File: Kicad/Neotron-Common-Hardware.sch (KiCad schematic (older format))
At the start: 17 parts, among them J101 Neotron-Expansion-Slot, J102 Neotron-Expansion-Slot, J103 Neotron-Expansion-Slot, J104 Neotron-Expansion-Slot, U101 Neotron-CPU

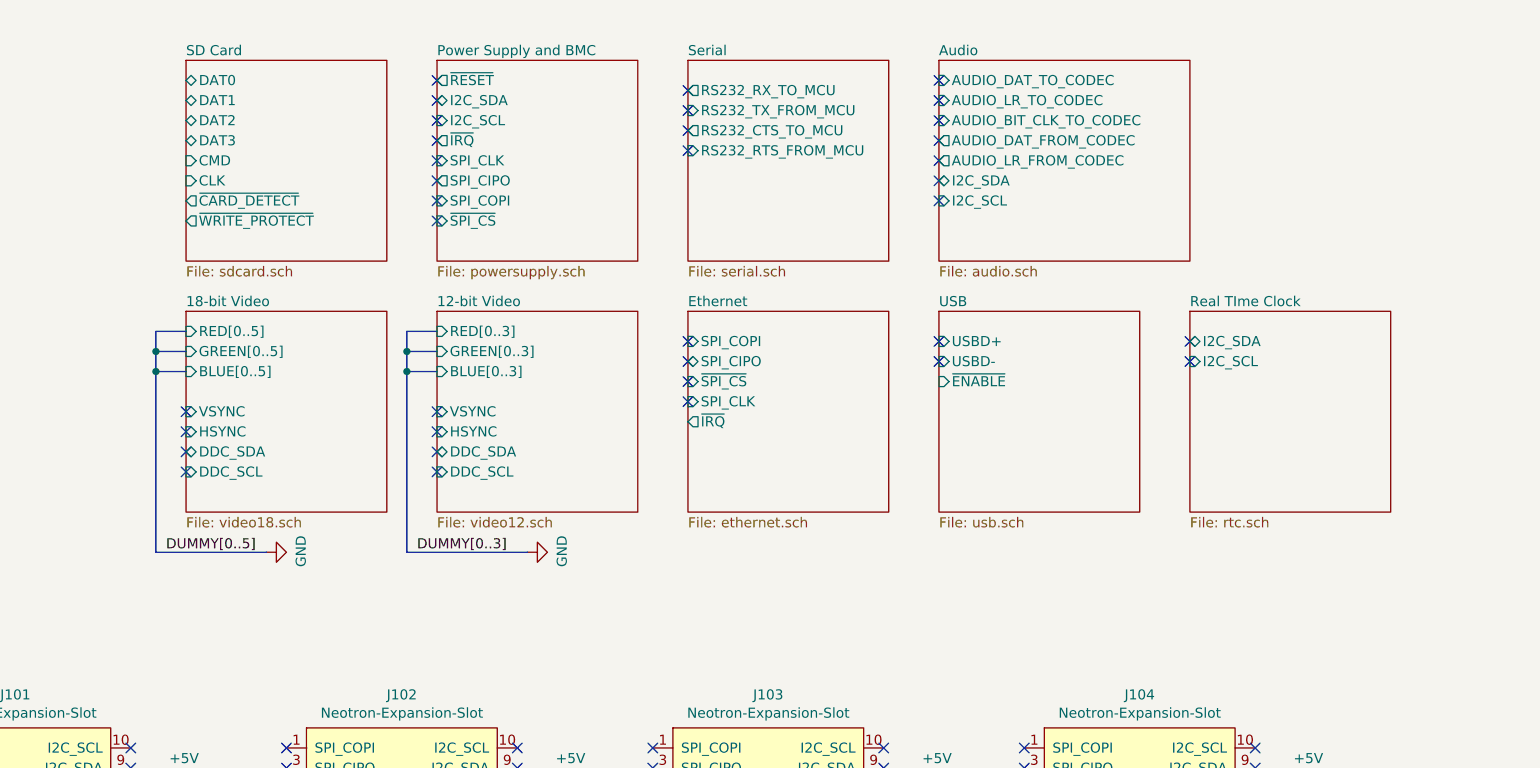
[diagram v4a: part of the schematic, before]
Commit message: Changes to BMC
* Swapped BUTTON_PWR and SYS_RESET to avoid DRC issue
* Split PSU and BMC into two separate sheets
* Swapped some pins on the STM32 to make it compatible with more
alternatives
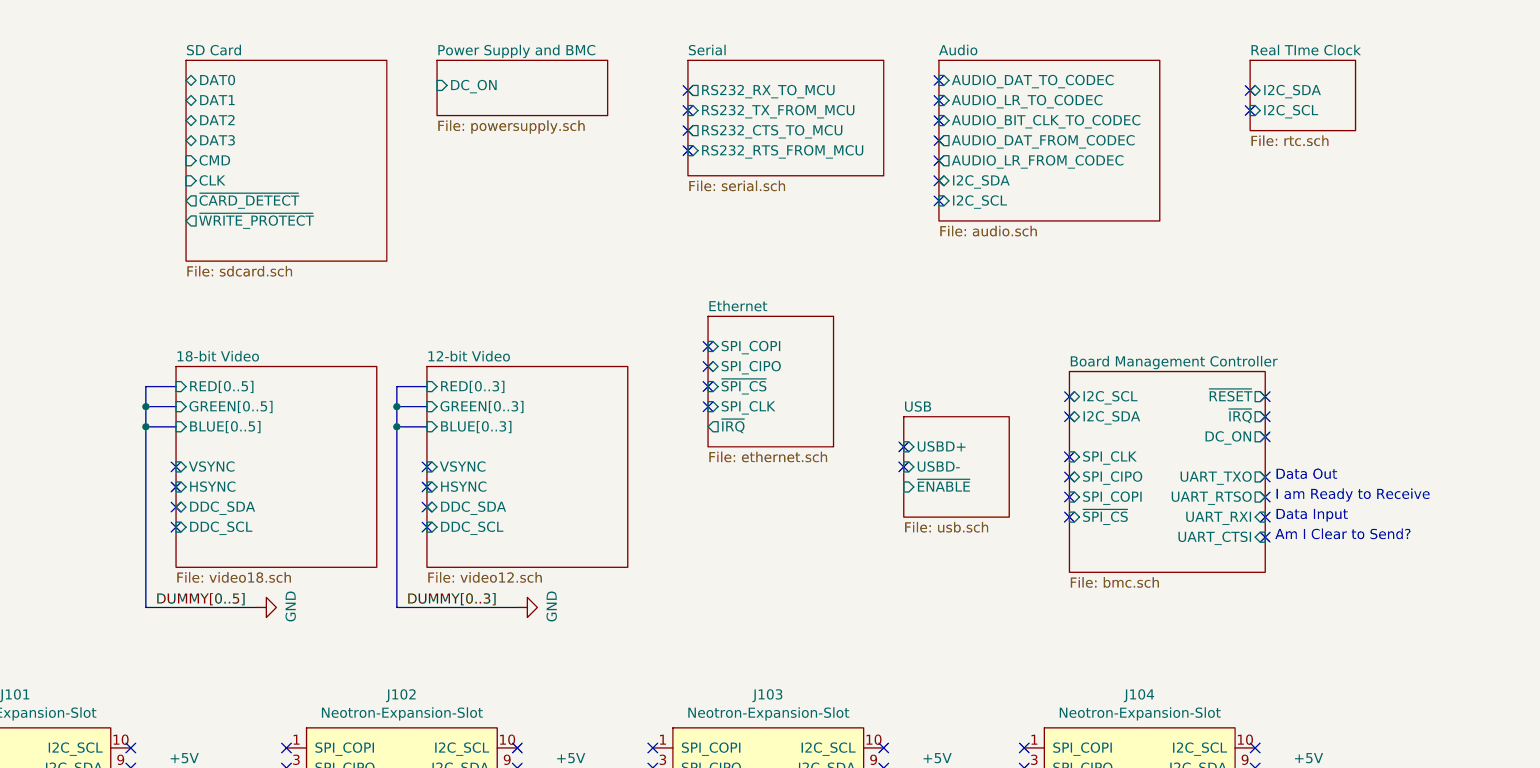
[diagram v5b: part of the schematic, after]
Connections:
- no-connect marks 132 -> 137
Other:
- note added: "Am I Clear to Send?"
- note added: "Data Input"
- note added: "Data Out"
- note added: "I am Ready to Receive"
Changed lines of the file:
@@
 $Descr A4 11693 8268
 encoding utf-8
-Sheet 1 16
+Sheet 1 17
 Title "Neotron Common Hardware"
 Date "2021-04-02"
@@
 $EndDescr
 $Sheet
-S 4850 2050 1000 1000
+S 4800 2325 1000 1000
 U 5FDE658D
 F0 "18-bit Video" 50
 F1 "video18.sch" 50
-F2 "DDC_SDA" B L 4850 2750 50
-F3 "DDC_SCL" I L 4850 2850 50
-F4 "VSYNC" I L 4850 2550 50
-F5 "HSYNC" I L 4850 2650 50
-F6 "RED[0..5]" I L 4850 2150 50
-F7 "GREEN[0..5]" I L 4850 2250 50
-F8 "BLUE[0..5]" I L 4850 2350 50
+F2 "DDC_SDA" B L 4800 3025 50
+F3 "DDC_SCL" I L 4800 3125 50
+F4 "VSYNC" I L 4800 2825 50
+F5 "HSYNC" I L 4800 2925 50
+F6 "RED[0..5]" I L 4800 2425 50
+F7 "GREEN[0..5]" I L 4800 2525 50
+F8 "BLUE[0..5]" I L 4800 2625 50
 $EndSheet
 $Sheet
-S 8600 800  1250 1000
+S 8600 800  1100 800
 U 5FDE6C5A
 F0 "Audio" 50
@@
 NoConn ~ 8600 1400
 NoConn ~ 8600 1500
-NoConn ~ 7350 2300
-NoConn ~ 7350 2400
-NoConn ~ 7350 2500
-NoConn ~ 7350 2200
+NoConn ~ 7450 2325
+NoConn ~ 7450 2425
+NoConn ~ 7450 2525
+NoConn ~ 7450 2225
 $Comp
 L Mechanical:MountingHole_Pad H102
@@
 	1    0    0    -1
 $EndComp
-NoConn ~ 8600 2200
-NoConn ~ 8600 2300
+NoConn ~ 8425 2725
+NoConn ~ 8425 2825
 $Sheet
 S 4850 800  1000 1000
@@
 	-1   0    0    -1
 $EndComp
-NoConn ~ 6100 1200
-NoConn ~ 6100 1100
-NoConn ~ 6100 1000
-NoConn ~ 6100 900
 NoConn ~ 7350 1250
 NoConn ~ 7350 1150
@@
 NoConn ~ 7350 950
 $Sheet
-S 7350 800  1000 1000
+S 7350 800  975  575
 U 5FDF53DB
 F0 "Serial" 50
@@
 $EndSheet
 $Sheet
-S 6100 800  1000 1000
-U 5FDE7599
-F0 "Power Supply and BMC" 50
-F1 "powersupply.sch" 50
-F2 "~RESET" O L 6100 900 50
-F3 "I2C_SDA" B L 6100 1000 50
-F4 "I2C_SCL" I L 6100 1100 50
-F5 "~IRQ" O L 6100 1200 50
-F6 "SPI_CLK" I L 6100 1300 50
-F7 "SPI_CIPO" O L 6100 1400 50
-F8 "SPI_COPI" I L 6100 1500 50
-F9 "~SPI_CS" I L 6100 1600 50
-$EndSheet
-$Sheet
-S 8600 2050 1000 1000
+S 8425 2575 525  500
 U 5FDE7004
 F0 "USB" 50
 F1 "usb.sch" 50
-F2 "USBD+" I L 8600 2200 50
-F3 "USBD-" I L 8600 2300 50
-F4 "~ENABLE" I L 8600 2400 50
+F2 "USBD+" I L 8425 2725 50
+F3 "USBD-" I L 8425 2825 50
+F4 "~ENABLE" I L 8425 2925 50
 $EndSheet
 $Sheet
-S 7350 2050 1000 1000
+S 7450 2075 625  650
 U 5FDE698D
 F0 "Ethernet" 50
 F1 "ethernet.sch" 50
-F2 "SPI_COPI" I L 7350 2200 50
-F3 "~SPI_CS" I L 7350 2400 50
-F4 "SPI_CLK" I L 7350 2500 50
-F5 "~IRQ" O L 7350 2600 50
-F6 "SPI_CIPO" T L 7350 2300 50
+F2 "SPI_COPI" I L 7450 2225 50
+F3 "~SPI_CS" I L 7450 2425 50
+F4 "SPI_CLK" I L 7450 2525 50
+F5 "~IRQ" O L 7450 2625 50
+F6 "SPI_CIPO" T L 7450 2325 50
 $EndSheet
 $Comp
@@
 NoConn ~ 3875 1250
 NoConn ~ 3875 1350
-NoConn ~ 4850 2550
-NoConn ~ 4850 2650
-NoConn ~ 4850 2750
-NoConn ~ 4850 2850
+NoConn ~ 4800 2825
+NoConn ~ 4800 2925
+NoConn ~ 4800 3025
+NoConn ~ 4800 3125
 NoConn ~ 2150 3675
 NoConn ~ 2575 3375
@@
 Connection ~ 4825 4525
 $Comp
-L power:+3V3 #PWR0118
+L power:+3V3 #PWR0117
 U 1 1 5FED8E4E
 P 4975 4625
-F 0 "#PWR0118" H 4975 4475 50  0001 C CNN
+F 0 "#PWR0117" H 4975 4475 50  0001 C CNN
 F 1 "+3V3" H 4990 4798 50  0000 C CNN
 F 2 "" H 4975 4625 50  0001 C CNN
@@
 $EndComp
 $Comp
-L power:GND #PWR0119
+L power:GND #PWR0118
 U 1 1 5FEDE866
 P 5200 5350
-F 0 "#PWR0119" H 5200 5100 50  0001 C CNN
+F 0 "#PWR0118" H 5200 5100 50  0001 C CNN
 F 1 "GND" H 5205 5177 50  0000 C CNN
 F 2 "" H 5200 5350 50  0001 C CNN
@@
 NoConn ~ 6200 6100
 $Sheet
-S 9850 2050 1000 1000
+S 10150 800  525  350
 U 5FEF404D
 F0 "Real TIme Clock" 50
 F1 "rtc.sch" 50
-F2 "I2C_SDA" B L 9850 2200 50
-F3 "I2C_SCL" I L 9850 2300 50
+F2 "I2C_SDA" B L 10150 950 50
+F3 "I2C_SCL" I L 10150 1050 50
 $EndSheet
-NoConn ~ 9850 2200
-NoConn ~ 9850 2300
+NoConn ~ 10150 950
+NoConn ~ 10150 1050
 $Sheet
-S 6100 2050 1000 1000
+S 6050 2325 1000 1000
 U 60677AF0
 F0 "12-bit Video" 50
 F1 "video12.sch" 50
-F2 "DDC_SDA" B L 6100 2750 50
-F3 "DDC_SCL" I L 6100 2850 50
-F4 "VSYNC" I L 6100 2550 50
-F5 "HSYNC" I L 6100 2650 50
-F6 "RED[0..3]" I L 6100 2150 50
-F7 "GREEN[0..3]" I L 6100 2250 50
-F8 "BLUE[0..3]" I L 6100 2350 50
+F2 "DDC_SDA" B L 6050 3025 50
+F3 "DDC_SCL" I L 6050 3125 50
+F4 "VSYNC" I L 6050 2825 50
+F5 "HSYNC" I L 6050 2925 50
+F6 "RED[0..3]" I L 6050 2425 50
+F7 "GREEN[0..3]" I L 6050 2525 50
+F8 "BLUE[0..3]" I L 6050 2625 50
 $EndSheet
-NoConn ~ 6100 2850
-NoConn ~ 6100 2750
-NoConn ~ 6100 2550
-NoConn ~ 6100 2650
+NoConn ~ 6050 3125
+NoConn ~ 6050 3025
+NoConn ~ 6050 2825
+NoConn ~ 6050 2925
 Wire Bus Line
-	6100 2150 5950 2150
+	6050 2425 5900 2425
 Wire Bus Line
-	5950 2150 5950 2250
+	5900 2425 5900 2525
 Wire Bus Line
-	5950 3250 6550 3250
+	5900 3525 6500 3525
 $Comp
 L power:GND #PWR0121
 U 1 1 606B5F3A
-P 6550 3250
-F 0 "#PWR0121" H 6550 3000 50  0001 C CNN
-F 1 "GND" H 6555 3077 50  0000 C CNN
-F 2 "" H 6550 3250 50  0001 C CNN
-F 3 "" H 6550 3250 50  0001 C CNN
-	1    6550 3250
+P 6500 3525
+F 0 "#PWR0121" H 6500 3275 50  0001 C CNN
+F 1 "GND" H 6505 3352 50  0000 C CNN
+F 2 "" H 6500 3525 50  0001 C CNN
+F 3 "" H 6500 3525 50  0001 C CNN
+	1    6500 3525
 	0    -1   -1   0
 $EndComp
 Wire Bus Line
-	6100 2250 5950 2250
-Connection ~ 5950 2250
+	6050 2525 5900 2525
+Connection ~ 5900 2525
 Wire Bus Line
-	5950 2250 5950 2350
+	5900 2525 5900 2625
 Wire Bus Line
-	6100 2350 5950 2350
-Connection ~ 5950 2350
+	6050 2625 5900 2625
+Connection ~ 5900 2625
 Wire Bus Line
-	5950 2350 5950 3250
-Text Label 6000 3250 0    50   ~ 0
+	5900 2625 5900 3525
+Text Label 5950 3525 0    50   ~ 0
 DUMMY[0..3]
 $Comp
-L power:GND #PWR0117
+L power:GND #PWR0119
 U 1 1 606CBEF3
-P 5250 3250
-F 0 "#PWR0117" H 5250 3000 50  0001 C CNN
-F 1 "GND" H 5255 3077 50  0000 C CNN
-F 2 "" H 5250 3250 50  0001 C CNN
-F 3 "" H 5250 3250 50  0001 C CNN
-	1    5250 3250
+P 5200 3525
+F 0 "#PWR0119" H 5200 3275 50  0001 C CNN
+F 1 "GND" H 5205 3352 50  0000 C CNN
+F 2 "" H 5200 3525 50  0001 C CNN
+F 3 "" H 5200 3525 50  0001 C CNN
+	1    5200 3525
 	0    -1   -1   0
 $EndComp
 Wire Bus Line
-	4850 2150 4700 2150
+	4800 2425 4650 2425
 Wire Bus Line
-	4700 2150 4700 2250
+	4650 2425 4650 2525
 Wire Bus Line
-	4700 3250 5250 3250
-Text Label 4750 3250 0    50   ~ 0
+	4650 3525 5200 3525
+Text Label 4700 3525 0    50   ~ 0
 DUMMY[0..5]
 Wire Bus Line
-	4850 2250 4700 2250
-Connection ~ 4700 2250
+	4800 2525 4650 2525
+Connection ~ 4650 2525
 Wire Bus Line
-	4700 2250 4700 2350
+	4650 2525 4650 2625
 Wire Bus Line
-	4850 2350 4700 2350
-Connection ~ 4700 2350
+	4800 2625 4650 2625
+Connection ~ 4650 2625
 Wire Bus Line
-	4700 2350 4700 3250
-NoConn ~ 6100 1300
-NoConn ~ 6100 1400
-NoConn ~ 6100 1500
-NoConn ~ 6100 1600
+	4650 2625 4650 3525
+$Sheet
+S 9250 2350 975  1000
+U 606E253F
+F0 "Board Management Controller" 50
+F1 "bmc.sch" 50
+F2 "I2C_SCL" B L 9250 2475 50
+F3 "~RESET" O R 10225 2475 50
+F4 "I2C_SDA" B L 9250 2575 50
+F5 "SPI_CLK" I L 9250 2775 50
+F6 "SPI_CIPO" T L 9250 2875 50
+F7 "SPI_COPI" I L 9250 2975 50
+F8 "~SPI_CS" I L 9250 3075 50
+F9 "~IRQ" O R 10225 2575 50
+F10 "DC_ON" O R 10225 2675 50
+F11 "UART_TXO" O R 10225 2875 50
+F12 "UART_RXI" I R 10225 3075 50
+F13 "UART_RTSO" O R 10225 2975 50
+F14 "UART_CTSI" I R 10225 3175 50
+$EndSheet
+$Sheet
+S 6100 800  850  275
+U 5FDE7599
+F0 "Power Supply and BMC" 50
+F1 "powersupply.sch" 50
+F2 "DC_ON" I L 6100 925 50
+$EndSheet
+NoConn ~ 9250 2475
+NoConn ~ 9250 2575
+NoConn ~ 9250 2775
+NoConn ~ 9250 2875
+NoConn ~ 9250 2975
+NoConn ~ 9250 3075
+NoConn ~ 10225 2475
+NoConn ~ 10225 2575
+NoConn ~ 10225 2675
+NoConn ~ 10225 2875
+NoConn ~ 10225 2975
+NoConn ~ 10225 3075
+NoConn ~ 10225 3175
+Text Notes 10275 2900 0    50   ~ 0
+Data Out
+Text Notes 10275 3000 0    50   ~ 0
+I am Ready to Receive
+Text Notes 10275 3100 0    50   ~ 0
+Data Input
+Text Notes 10275 3200 0    50   ~ 0
+Am I Clear to Send?
 $EndSCHEMATC

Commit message: Set LR and BCLK on Audio.sch to be bi-directional
In Controller mode these pins are outputs. In peripheral
mode these pins are inputs.
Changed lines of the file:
@@
 F0 "Audio" 50
 F1 "audio.sch" 50
-F2 "AUDIO_DAT_TO_CODEC" I L 8600 900 50
-F3 "AUDIO_LR_TO_CODEC" I L 8600 1000 50
-F4 "AUDIO_BIT_CLK_TO_CODEC" I L 8600 1100 50
-F5 "AUDIO_DAT_FROM_CODEC" O L 8600 1200 50
-F6 "AUDIO_LR_FROM_CODEC" O L 8600 1300 50
-F7 "I2C_SDA" B L 8600 1400 50
-F8 "I2C_SCL" I L 8600 1500 50
+F2 "I2C_SDA" B L 8600 1400 50
+F3 "I2C_SCL" I L 8600 1500 50
+F4 "AUDIO_DAC_DAT" I L 8600 900 50
+F5 "AUDIO_DAC_LR" B L 8600 1000 50
+F6 "AUDIO_BIT_CLK" B L 8600 1100 50
+F7 "AUDIO_ADC_DATA" O L 8600 1200 50
+F8 "AUDIO_ADC_LR" B L 8600 1300 50
 $EndSheet
 NoConn ~ 8600 900

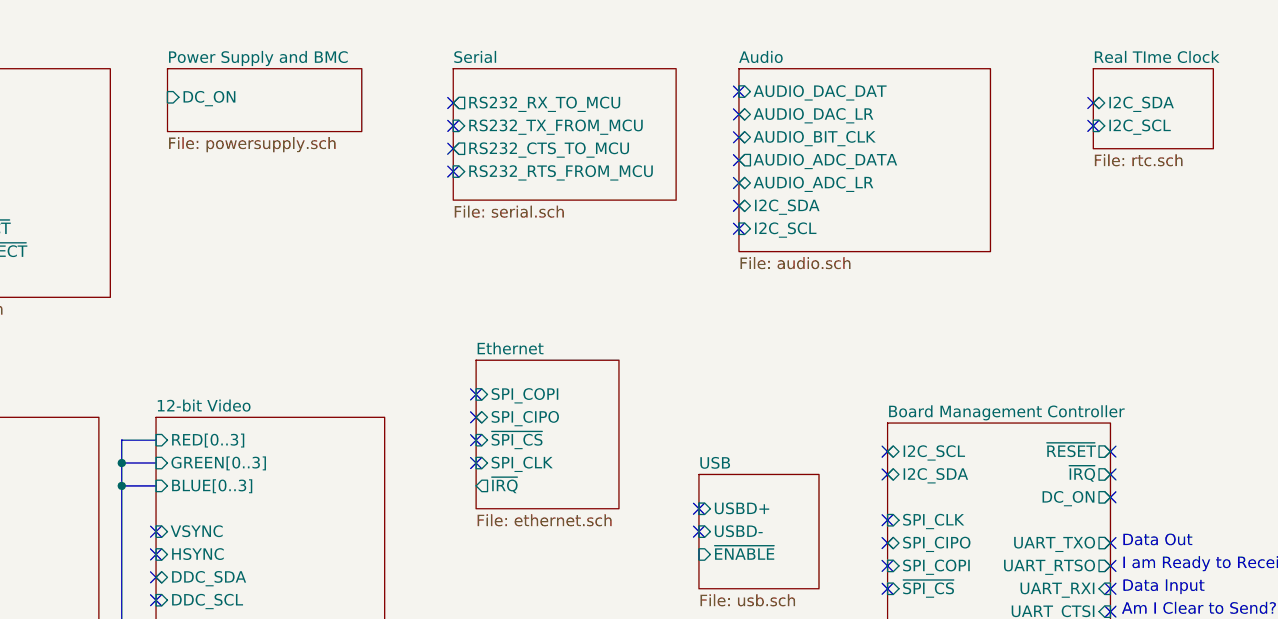
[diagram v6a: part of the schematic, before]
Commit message: Revised PSU switch-on circuit.
Updated notes on BMC and Audio sheet.
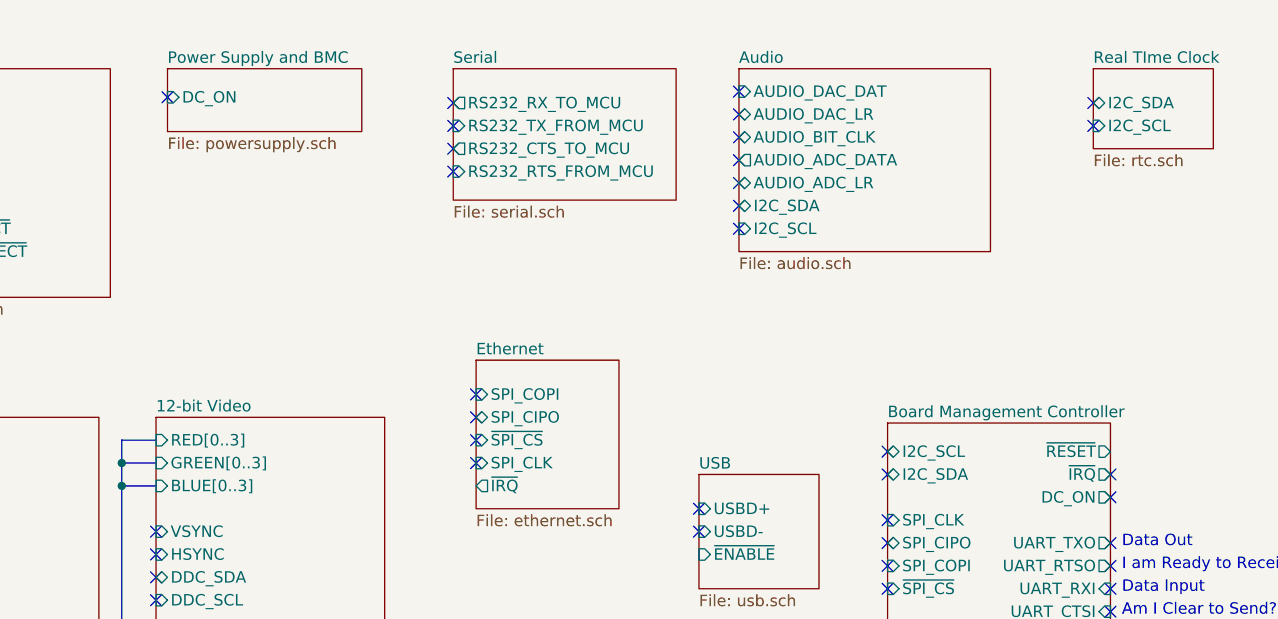
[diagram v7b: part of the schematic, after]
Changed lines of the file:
@@
 Sheet 1 17
 Title "Neotron Common Hardware"
-Date "2021-04-02"
+Date "2021-04-06"
 Rev "[Uncontrolled]"
 Comp "https://neotron-compute.github.io/"
@@
 NoConn ~ 9250 2975
 NoConn ~ 9250 3075
-NoConn ~ 10225 2475
 NoConn ~ 10225 2575
 NoConn ~ 10225 2675
@@
 Text Notes 10275 3200 0    50   ~ 0
 Am I Clear to Send?
+NoConn ~ 6100 925
 $EndSCHEMATC

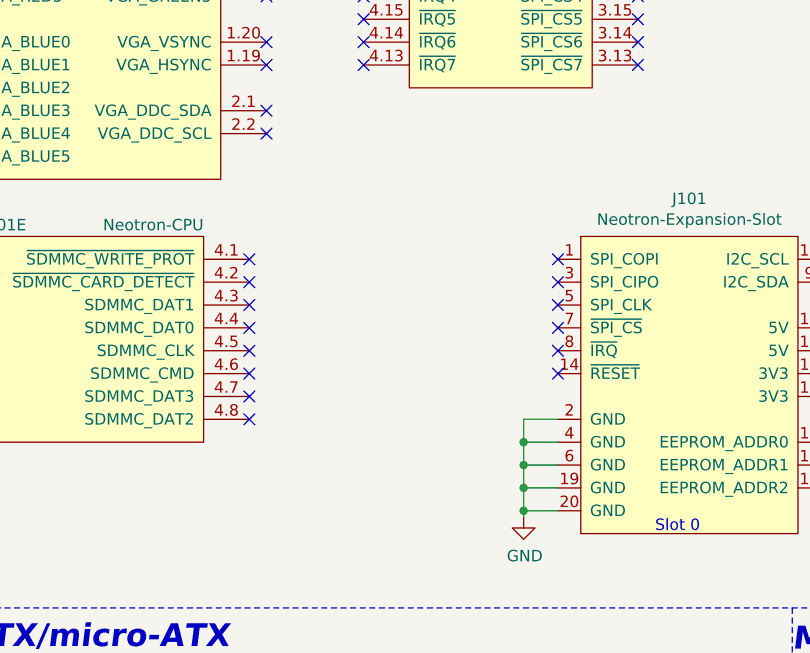
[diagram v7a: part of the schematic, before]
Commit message: Brought in sheets from Neotron Pico.
Also includes DB15HD and PSU 3D models.
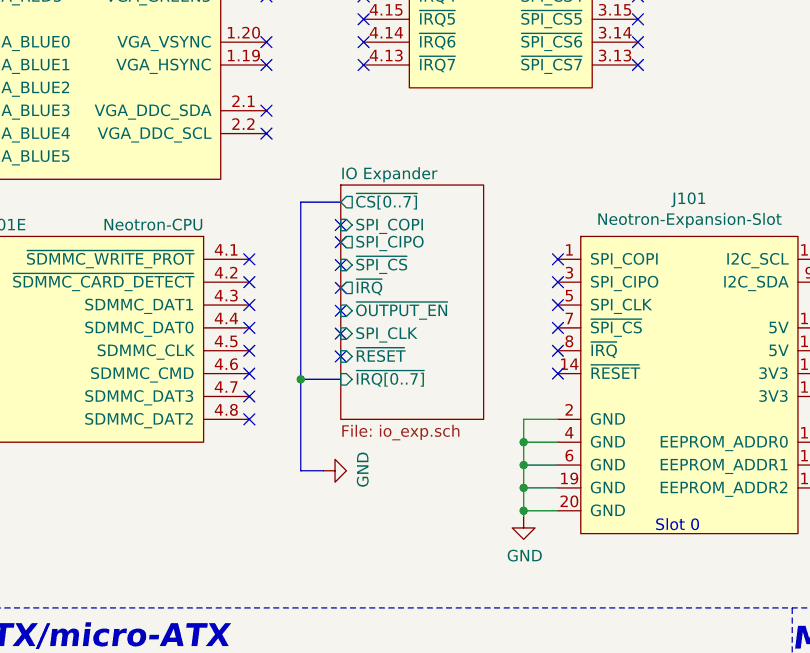
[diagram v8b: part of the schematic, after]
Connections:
- no-connect marks 137 -> 144
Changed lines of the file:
@@
 $Descr A4 11693 8268
 encoding utf-8
-Sheet 1 17
+Sheet 1 18
 Title "Neotron Common Hardware"
-Date "2021-04-06"
+Date "2021-06-18"
 Rev "[Uncontrolled]"
 Comp "https://neotron-compute.github.io/"
@@
 $EndComp
 $Comp
-L power:GND #PWR0118
+L power:GND #PWR0119
 U 1 1 5FEDE866
 P 5200 5350
-F 0 "#PWR0118" H 5200 5100 50  0001 C CNN
+F 0 "#PWR0119" H 5200 5100 50  0001 C CNN
 F 1 "GND" H 5205 5177 50  0000 C CNN
 F 2 "" H 5200 5350 50  0001 C CNN
@@
 DUMMY[0..3]
 $Comp
-L power:GND #PWR0119
+L power:GND #PWR0118
 U 1 1 606CBEF3
 P 5200 3525
-F 0 "#PWR0119" H 5200 3275 50  0001 C CNN
+F 0 "#PWR0118" H 5200 3275 50  0001 C CNN
 F 1 "GND" H 5205 3352 50  0000 C CNN
 F 2 "" H 5200 3525 50  0001 C CNN
@@
 Am I Clear to Send?
 NoConn ~ 6100 925
+$Sheet
+S 2475 3900 625  1025
+U 60CCE28A
+F0 "IO Expander" 50
+F1 "io_exp.sch" 50
+F2 "~CS[0..7]" O L 2475 3975 50
+F3 "SPI_COPI" I L 2475 4075 50
+F4 "SPI_CIPO" O L 2475 4150 50
+F5 "~SPI_CS" I L 2475 4250 50
+F6 "~IRQ" O L 2475 4350 50
+F7 "~OUTPUT_EN" I L 2475 4450 50
+F8 "SPI_CLK" I L 2475 4550 50
+F9 "~RESET" I L 2475 4650 50
+F10 "~IRQ[0..7]" I L 2475 4750 50
+$EndSheet
+NoConn ~ 2475 4075
+NoConn ~ 2475 4150
+NoConn ~ 2475 4250
+NoConn ~ 2475 4350
+NoConn ~ 2475 4450
+NoConn ~ 2475 4550
+NoConn ~ 2475 4650
+Wire Bus Line
+	2475 3975 2300 3975
+Wire Bus Line
+	2300 3975 2300 4750
+Wire Bus Line
+	2300 4750 2475 4750
+Wire Bus Line
+	2300 4750 2300 5150
+Wire Bus Line
+	2300 5150 2400 5150
+Connection ~ 2300 4750
+$Comp
+L power:GND #PWR0133
+U 1 1 60D12FF7
+P 2400 5150
+F 0 "#PWR0133" H 2400 4900 50  0001 C CNN
+F 1 "GND" H 2405 4977 50  0000 C CNN
+F 2 "" H 2400 5150 50  0001 C CNN
+F 3 "" H 2400 5150 50  0001 C CNN
+	1    2400 5150
+	0    -1   -1   0
+$EndComp
 $EndSCHEMATC
